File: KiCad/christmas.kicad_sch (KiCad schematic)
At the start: 26 parts, among them J1 Conn_01x04, J2 Conn_01x04, J3 Batery_9V, U2 4015

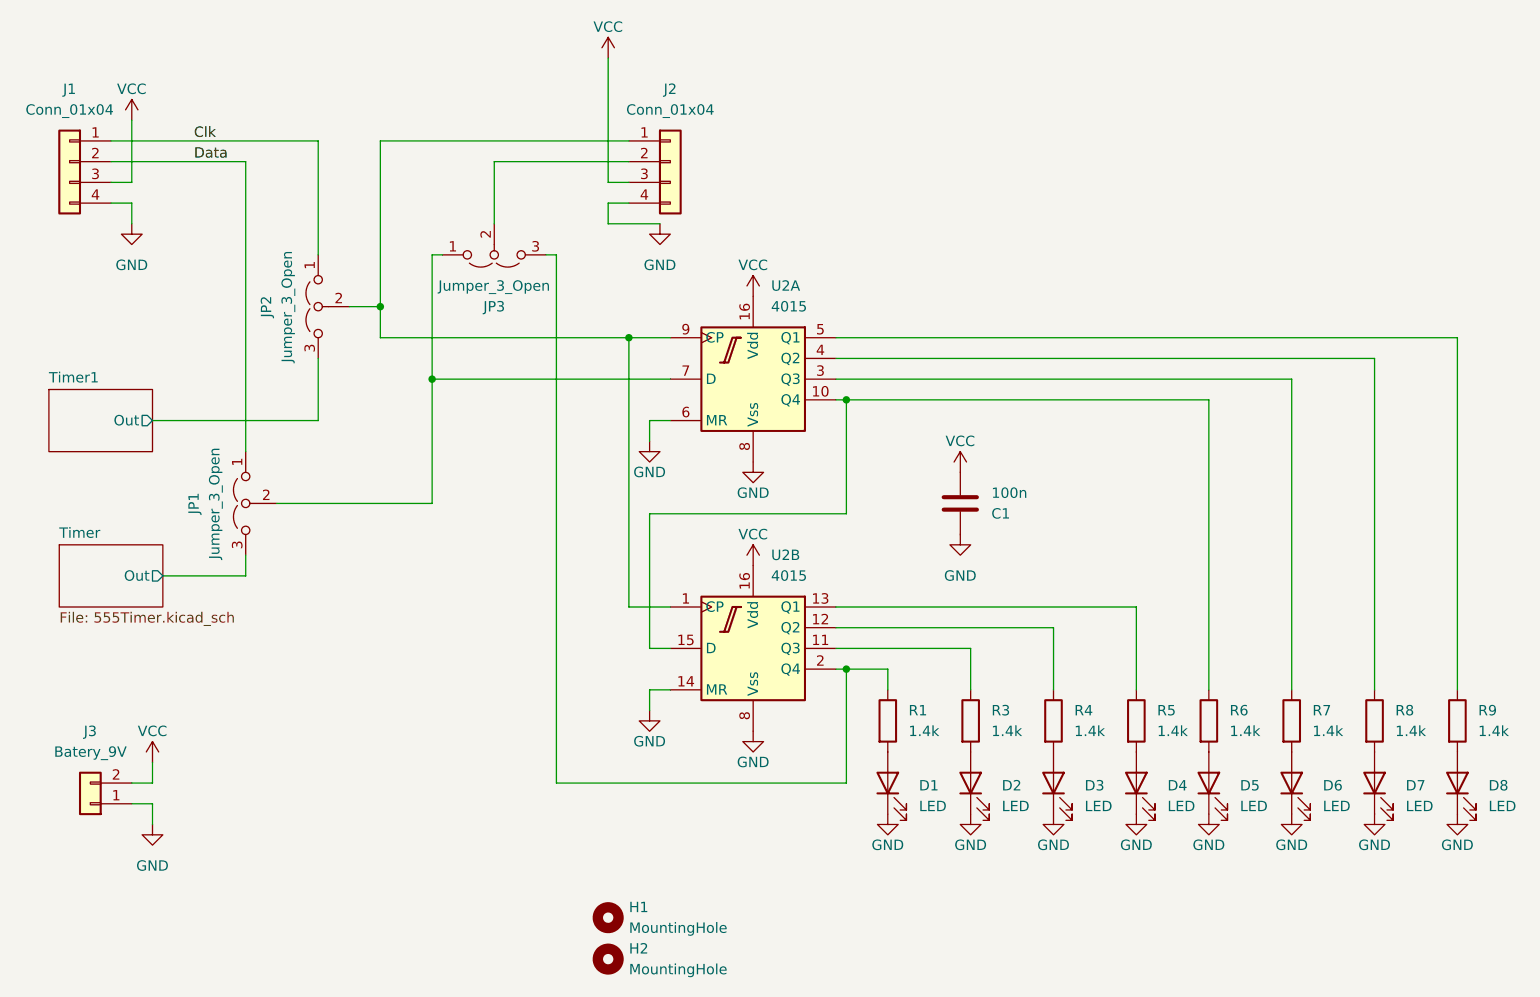
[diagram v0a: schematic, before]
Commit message: rewire board2board connector to match "same direction" cables
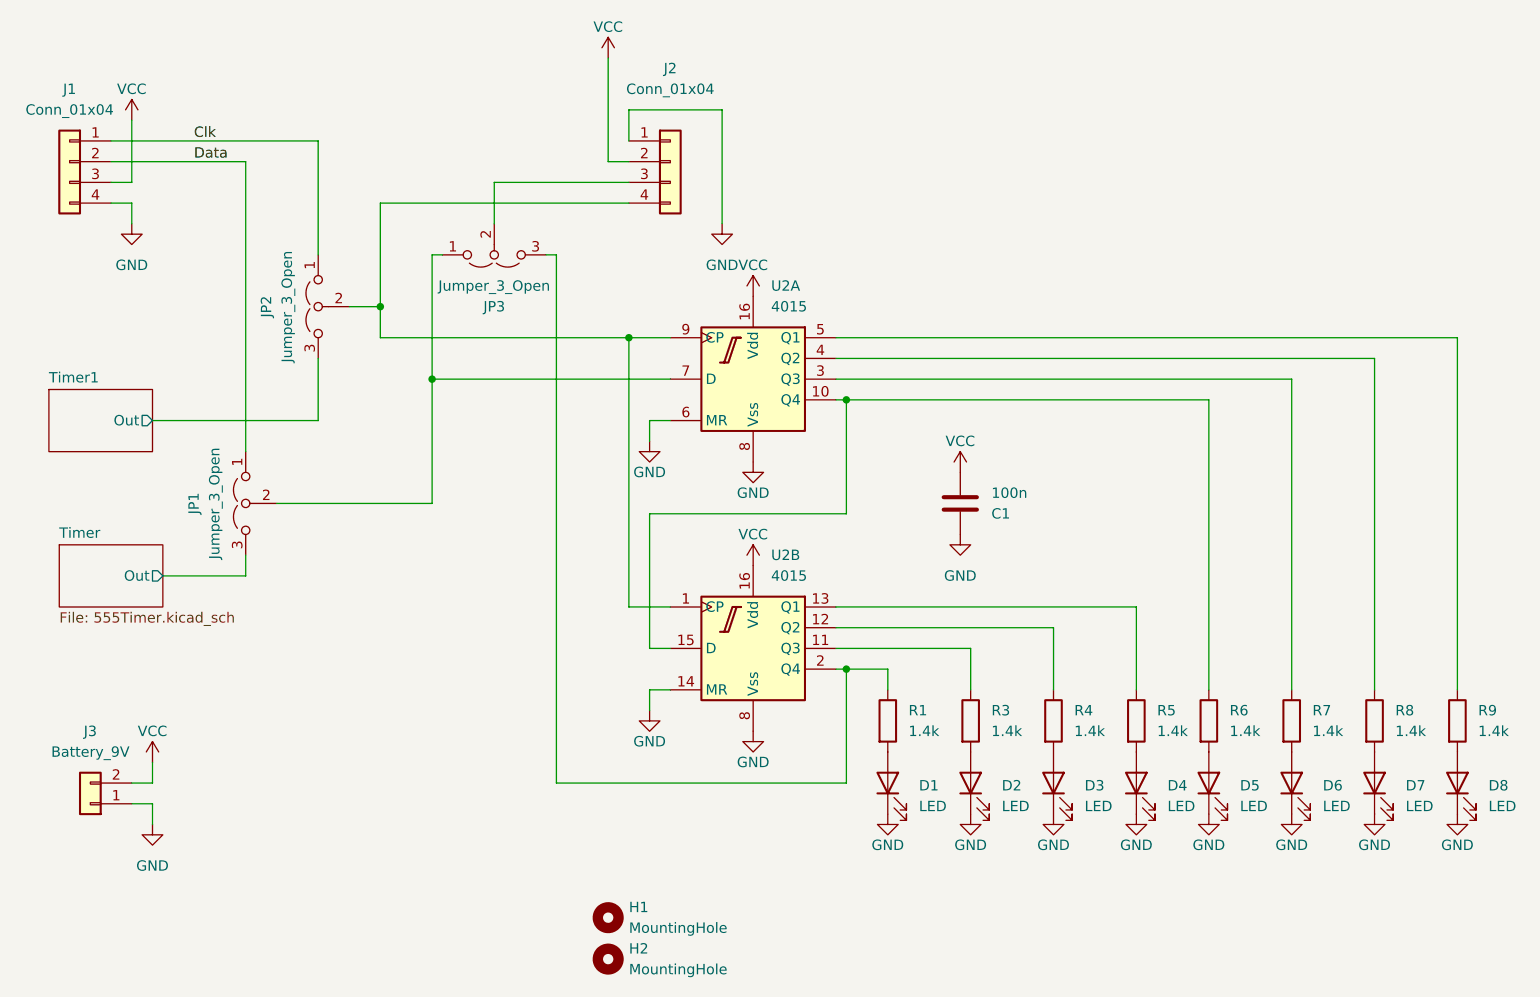
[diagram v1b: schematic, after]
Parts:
- J3: value Batery_9V -> Battery_9V
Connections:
- net GND: now also J2.1 (Pin_1); no longer J2.4 (Pin_4)
- net VCC: now also J2.2 (Pin_2); no longer J2.3 (Pin_3)
- net at JP2.2 (C), U2.1 (CP), U2.9 (CP): now also J2.4 (Pin_4); no longer J2.1 (Pin_1)
- net at JP3.2 (C): now also J2.3 (Pin_3); no longer J2.2 (Pin_2)
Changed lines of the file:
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@@
-    (stroke (width 0) (type default))
-  )
-  (wire (pts (xy 114.3 66.04) (xy 116.84 66.04))
     (stroke (width 0) (type default))
   )
@@
     (stroke (width 0) (type default))
   )
-  (wire (pts (xy 114.3 48.26) (xy 114.3 63.5))
-    (stroke (width 0) (type default))
-  )
   (wire (pts (xy 119.38 120.65) (xy 121.92 120.65))
     (stroke (width 0) (type default))
@@
     (stroke (width 0) (type default))
   )
+  (wire (pts (xy 116.84 66.04) (xy 86.36 66.04))
+    (stroke (width 0) (type default))
+  )
+  (wire (pts (xy 100.33 63.5) (xy 116.84 63.5))
+    (stroke (width 0) (type default))
+  )
   (wire (pts (xy 86.36 82.55) (xy 116.84 82.55))
     (stroke (width 0) (type default))
@@
     (stroke (width 0) (type default))
   )
+  (wire (pts (xy 114.3 60.96) (xy 116.84 60.96))
+    (stroke (width 0) (type default))
+  )
   (wire (pts (xy 143.51 123.19) (xy 143.51 137.16))
     (stroke (width 0) (type default))
@@
     (stroke (width 0) (type default))
   )
-  (wire (pts (xy 86.36 58.42) (xy 86.36 78.74))
-    (stroke (width 0) (type default))
-  )
   (wire (pts (xy 116.84 82.55) (xy 116.84 115.57))
     (stroke (width 0) (type default))
   )
-  (wire (pts (xy 100.33 60.96) (xy 116.84 60.96))
-    (stroke (width 0) (type default))
-  )
-  (wire (pts (xy 100.33 68.58) (xy 100.33 60.96))
-    (stroke (width 0) (type default))
-  )
   (wire (pts (xy 142.24 85.09) (xy 208.28 85.09))
     (stroke (width 0) (type default))
   )
+  (wire (pts (xy 100.33 68.58) (xy 100.33 63.5))
+    (stroke (width 0) (type default))
+  )
   (wire (pts (xy 86.36 78.74) (xy 86.36 82.55))
     (stroke (width 0) (type default))
@@
     (stroke (width 0) (type default))
   )
-  (wire (pts (xy 114.3 68.58) (xy 120.65 68.58))
-    (stroke (width 0) (type default))
-  )
   (wire (pts (xy 78.74 92.71) (xy 78.74 85.09))
     (stroke (width 0) (type default))
@@
     (stroke (width 0) (type default))
   )
+  (wire (pts (xy 128.27 68.58) (xy 128.27 54.61))
+    (stroke (width 0) (type default))
+  )
   (wire (pts (xy 53.34 60.96) (xy 69.85 60.96))
     (stroke (width 0) (type default))
@@
     (stroke (width 0) (type default))
   )
-  (wire (pts (xy 114.3 68.58) (xy 114.3 66.04))
-    (stroke (width 0) (type default))
-  )
   (wire (pts (xy 55.88 66.04) (xy 53.34 66.04))
     (stroke (width 0) (type default))
@@
     (stroke (width 0) (type default))
   )
+  (wire (pts (xy 116.84 54.61) (xy 116.84 58.42))
+    (stroke (width 0) (type default))
+  )
   (wire (pts (xy 119.38 128.27) (xy 119.38 125.73))
     (stroke (width 0) (type default))
@@
     (stroke (width 0) (type default))
   )
+  (wire (pts (xy 86.36 66.04) (xy 86.36 78.74))
+    (stroke (width 0) (type default))
+  )
   (wire (pts (xy 158.75 120.65) (xy 158.75 125.73))
     (stroke (width 0) (type default))
   )
-  (wire (pts (xy 86.36 58.42) (xy 116.84 58.42))
-    (stroke (width 0) (type default))
-  )
   (wire (pts (xy 143.51 123.19) (xy 148.59 123.19))
     (stroke (width 0) (type default))
@@
     (stroke (width 0) (type default))
   )
+  (wire (pts (xy 114.3 48.26) (xy 114.3 60.96))
+    (stroke (width 0) (type default))
+  )
   (wire (pts (xy 119.38 92.71) (xy 121.92 92.71))
     (stroke (width 0) (type default))
   )
-  (wire (pts (xy 114.3 63.5) (xy 116.84 63.5))
-    (stroke (width 0) (type default))
-  )
   (wire (pts (xy 55.88 63.5) (xy 53.34 63.5))
     (stroke (width 0) (type default))
@@
   )
   (wire (pts (xy 92.71 72.39) (xy 93.98 72.39))
+    (stroke (width 0) (type default))
+  )
+  (wire (pts (xy 128.27 54.61) (xy 116.84 54.61))
     (stroke (width 0) (type default))
   )
@@
   (symbol (lib_id "Connector_Generic:Conn_01x04") (at 121.92 60.96 0) (unit 1)
     (in_bom yes) (on_board yes) (dnp no)
-    (property "Reference" "J2" (at 121.92 52.07 0)
-      (effects (font (size 1.27 1.27)))
-    )
-    (property "Value" "Conn_01x04" (at 121.92 54.61 0)
+    (property "Reference" "J2" (at 121.92 49.53 0)
+      (effects (font (size 1.27 1.27)))
+    )
+    (property "Value" "Conn_01x04" (at 121.92 52.07 0)
       (effects (font (size 1.27 1.27)))
     )
@@
       (effects (font (size 1.27 1.27)))
     )
-    (property "Value" "Batery_9V" (at 50.8 133.35 0)
+    (property "Value" "Battery_9V" (at 50.8 133.35 0)
       (effects (font (size 1.27 1.27)))
     )
@@
     )
   )
-  (symbol (lib_id "power:GND") (at 120.65 68.58 0) (unit 1)
-    (in_bom yes) (on_board yes) (dnp no) (fields_autoplaced)
-    (property "Reference" "#PWR027" (at 120.65 74.93 0)
-      (effects (font (size 1.27 1.27)) hide)
-    )
-    (property "Value" "GND" (at 120.65 73.66 0)
-      (effects (font (size 1.27 1.27)))
-    )
-    (property "Footprint" "" (at 120.65 68.58 0)
-      (effects (font (size 1.27 1.27)) hide)
-    )
-    (property "Datasheet" "" (at 120.65 68.58 0)
-      (effects (font (size 1.27 1.27)) hide)
-    )
+  (symbol (lib_id "power:GND") (at 128.27 68.58 0) (unit 1)
+    (in_bom yes) (on_board yes) (dnp no) (fields_autoplaced)
+    (property "Reference" "#PWR027" (at 128.27 74.93 0)
+      (effects (font (size 1.27 1.27)) hide)
+    )
+    (property "Value" "GND" (at 128.27 73.66 0)
+      (effects (font (size 1.27 1.27)))
+    )
+    (property "Footprint" "" (at 128.27 68.58 0)
+      (effects (font (size 1.27 1.27)) hide)
+    )
+    (property "Datasheet" "" (at 128.27 68.58 0)
+      (effects (font (size 1.27 1.27)) hide)
+    )
